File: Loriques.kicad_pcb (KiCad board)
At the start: 4 copper layers, 144.8 x 106.7 mm, 131 parts, among them IC10 MAX17263LETD+T, IC12 TPS22975, IC14 W25Q64FWSSIG, IC19 TPS22975, IC2 MCP73871, IC3 HDC2080, IC4 TPS2013A, IC5 CAT25160VI-GT3, IC6 SN74LVC244A, IC7 LP38691-ADJ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

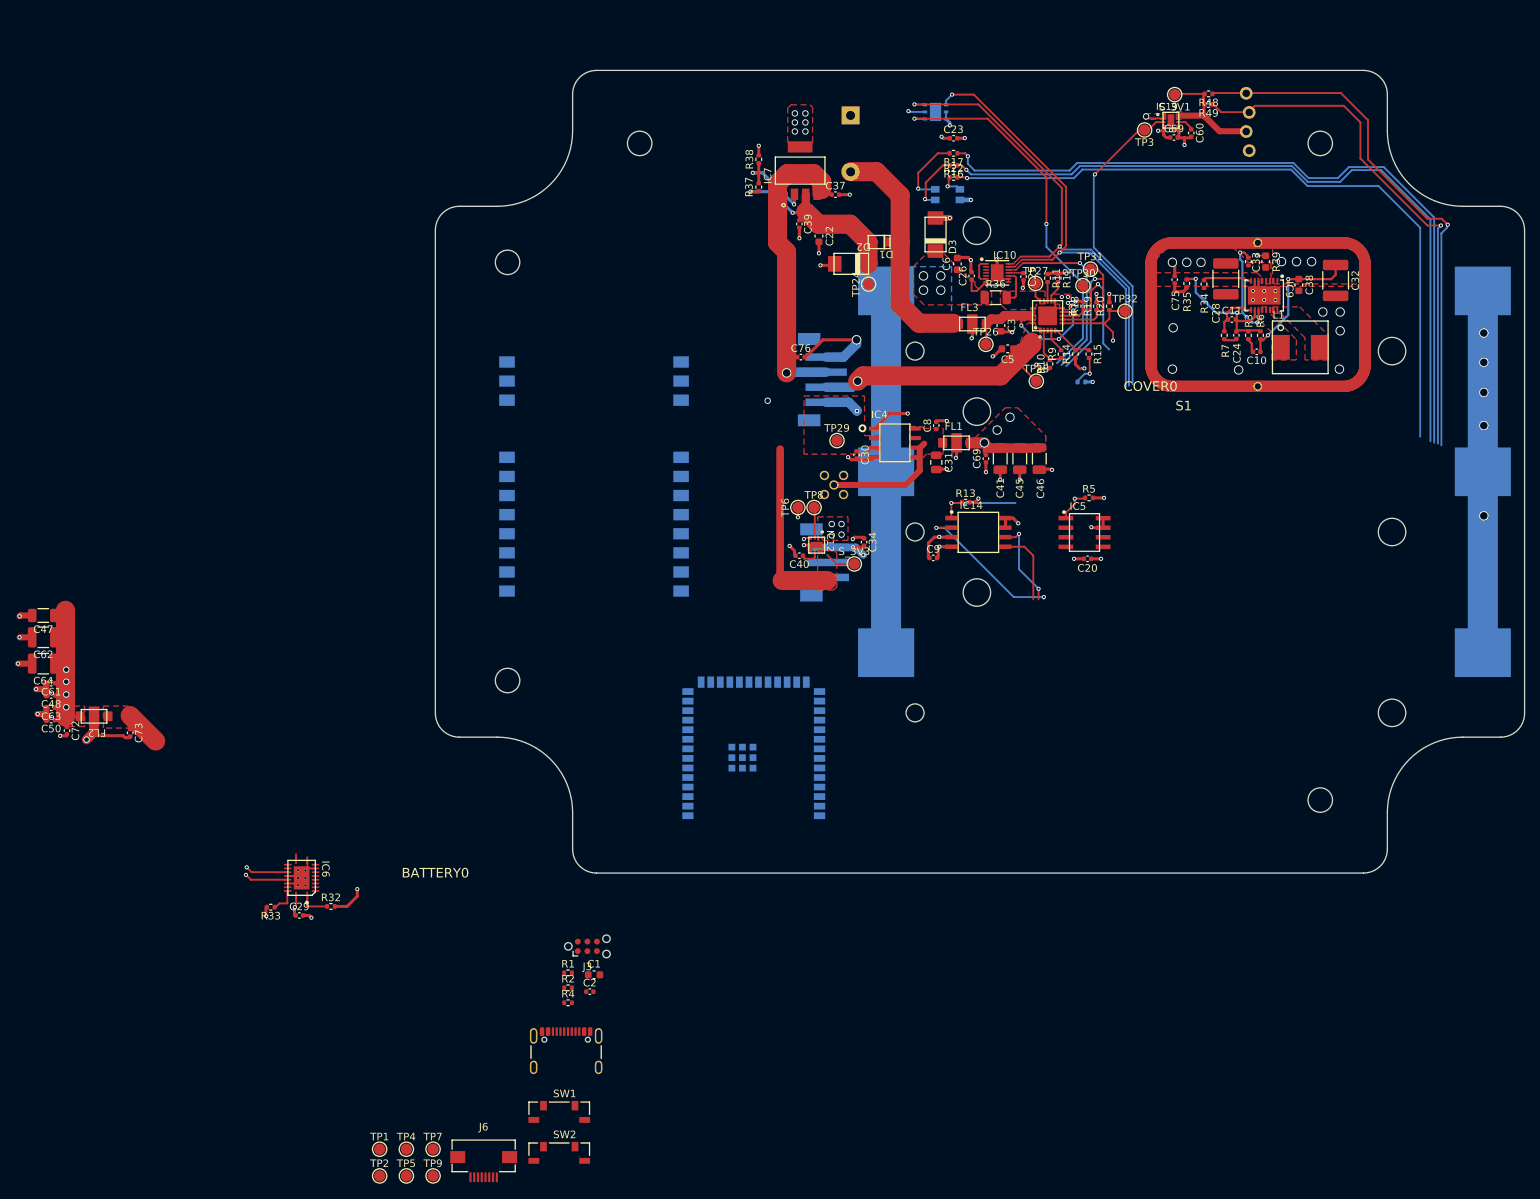
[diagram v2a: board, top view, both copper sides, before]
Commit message: more 3D parts. changed out the temp/humidity sensor for an instock one
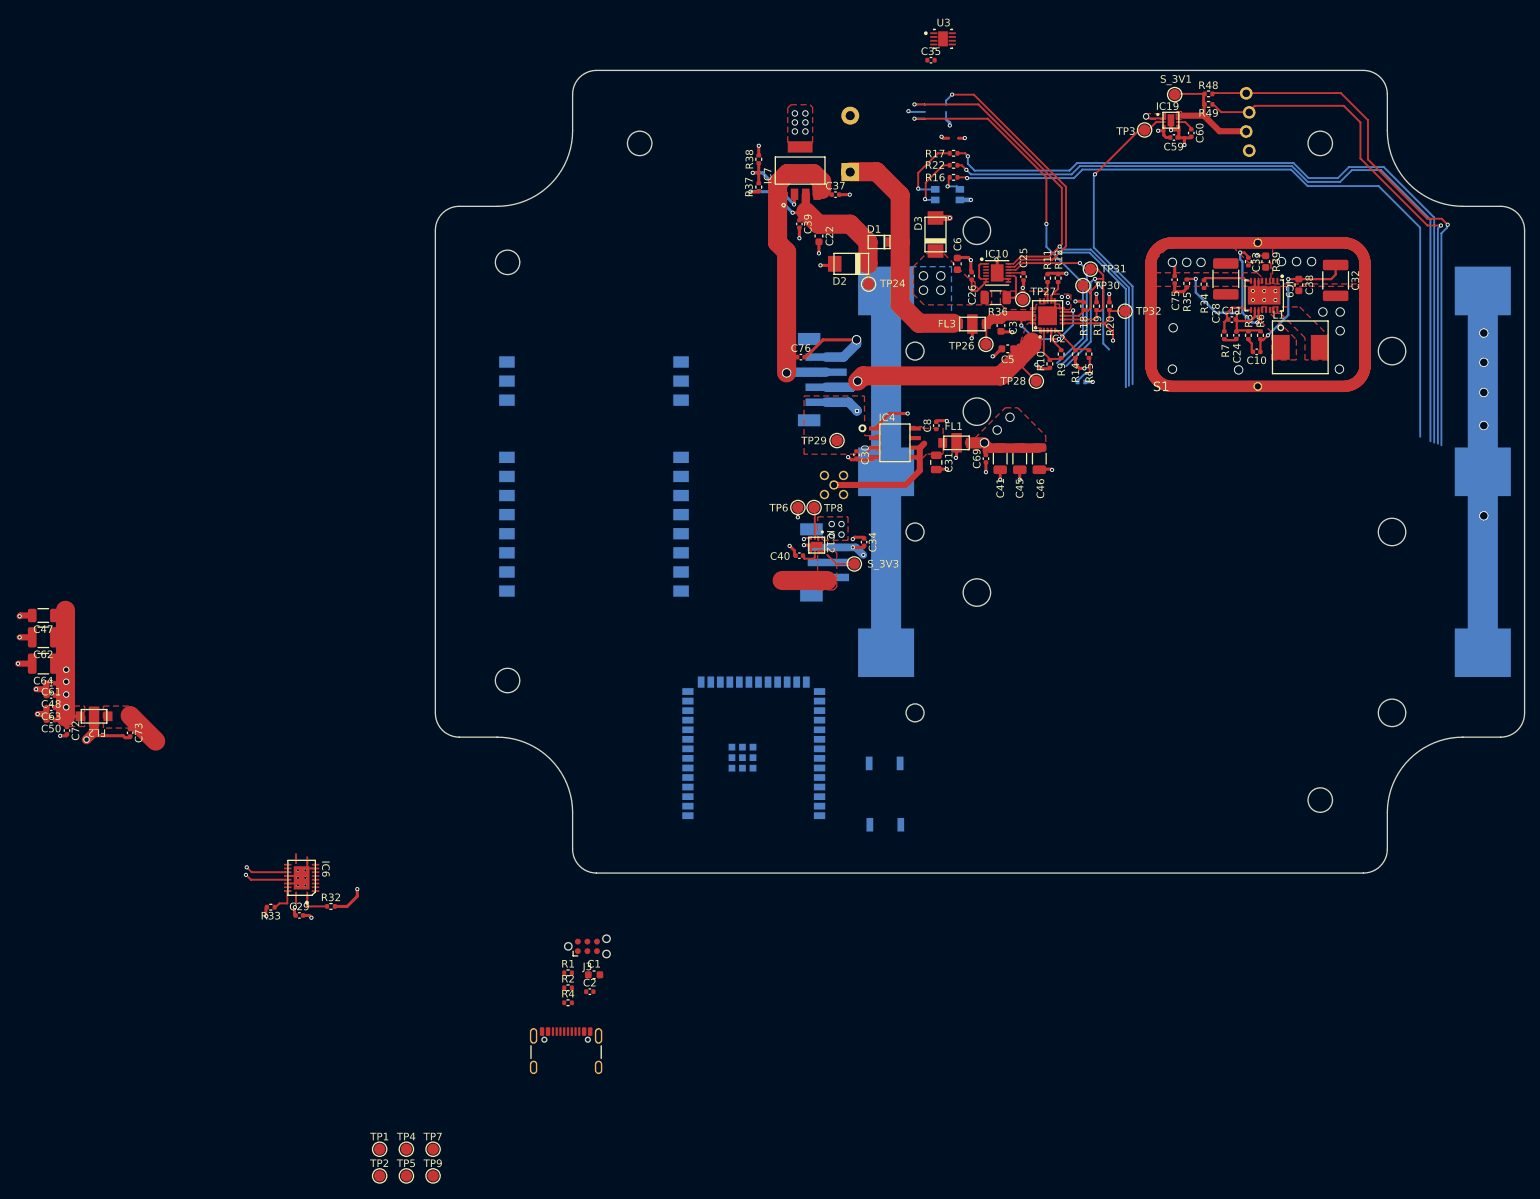
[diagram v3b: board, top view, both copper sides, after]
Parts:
- removed C20, C23, C9: 0.1uF, Capacitor_SMD:C_0402_1005Metric
- removed IC14: W25Q64FWSSIG, Loriques:SOIC127P790X216-8N
- removed IC3: HDC2080, Loriques:DMB0006A
- removed IC5: CAT25160VI-GT3, Loriques:SOIC127P600X175-8N
- removed J6: Conn_01x08, Loriques:FPC-SMD_P0.50-8P_FGS-XJ-H2.0
- removed R13, R5: 100k, Resistor_SMD:R_0402_1005Metric
- added C35: 0.1uF, Capacitor_SMD:C_0402_1005Metric, F.Cu at (142.0, 50.3)
- added U3: HDC3020DEFR, Loriques:DEF0008A-IPC_A, F.Cu at (143.6, 47.4)
- C27: value CPOL_16X27MM -> 4700uF
- SW1, SW2: footprint Loriques:SW_TL3330AF130QG_EWI -> Loriques:SW_CS1213AGF260_CRS; moved to B.Cu
- moved COVER0 73.0 mm to (174.8, 166.6)
- moved SW2 67.9 mm to (135.8, 143.8)
- moved SW1 58.2 mm to (135.9, 151.9)
- moved C27 7.53 mm to (131.2, 65.2), turned to 90 degrees
- moved TP27 2.72 mm to (154.2, 82.1)
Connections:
- C27 pad 1: (no net) -> Net-(C27-Pad1)
- C27 pad 2: (no net) -> GND
- D1 pad K: Net-(C27-Pad+) -> Net-(C27-Pad1)
- FL3 pad 1: Net-(C27-Pad+) -> Net-(C27-Pad1)
- IC6 pad P$11: /Radio/RXEN -> /Radio/RXEN_MCU
- IC6 pad P$12: /Radio/NSS -> /Radio/NSS_RADIO
- IC6 pad P$13: /Radio/TXEN -> /Radio/TXEN_MCU
- IC6 pad P$14: /Radio/SCK -> /Radio/SCK_RADIO
- IC6 pad P$15: /Radio/RST -> /Radio/RST_MCU
- IC6 pad P$16: /Radio/MOSI -> /Radio/MOSI_RADIO
- IC6 pad P$17: /Radio/BUSY -> /Radio/BUSY_RADIO
- IC6 pad P$18: /Radio/MISO -> /Radio/MISO_MCU
- IC6 pad P$2: /Radio/MISO -> /Radio/MISO_RADIO
- IC6 pad P$3: /Radio/BUSY -> /Radio/BUSY_MCU
- IC6 pad P$4: /Radio/MOSI -> /Radio/MOSI_MCU
- IC6 pad P$5: /Radio/RST -> /Radio/RST_RADIO
- IC6 pad P$6: /Radio/SCK -> /Radio/SCK_MCU
- IC6 pad P$7: /Radio/TXEN -> /Radio/TXEN_RADIO
- IC6 pad P$8: /Radio/NSS -> /Radio/NSS_MCU
- IC6 pad P$9: /Radio/RXEN -> /Radio/RXEN_RADIO
- U1 pad 10: /MCU/TX_3V3 -> /MCU/TX_DEBUG_O
- U1 pad 11: /MCU/RX_3V3 -> /MCU/RX_DEBUG_O
- U1 pad 12: unconnected-(U1-GPIO8/TOUCH8/ADC1_CH7/SUBSPICS1-Pad12) -> /MCU/STAT2
- U1 pad 15: unconnected-(U1-GPIO3/TOUCH3/ADC1_CH2*-Pad15) -> /Radio/RXEN_MCU
- U1 pad 17: unconnected-(U1-GPIO9/TOUCH9/ADC1_CH8/FSPIHD/SUBSPIHD-Pad17) -> /MCU/STAT1
- U1 pad 18: unconnected-(U1-GPIO10/TOUCH10/ADC1_CH9/FSPICS0/FSPIIO4/SUBSPICS0-Pad18) -> /Radio/NSS_MCU
- U1 pad 19: unconnected-(U1-GPIO11/TOUCH11/ADC2_CH0/FSPID/FSPIIO5/SUBSPID-Pad19) -> /Radio/MOSI_MCU
- U1 pad 20: unconnected-(U1-GPIO12/TOUCH12/ADC2_CH1/FSPICLK/FSPIIO6/SUBSPICLK-Pad20) -> /Radio/SCK_MCU
- U1 pad 21: unconnected-(U1-GPIO13/TOUCH13/ADC2_CH2/FSPIQ/FSPIIO7/SUBSPIQ-Pad21) -> /Radio/MISO_MCU
- U1 pad 32: Net-(J6-Pin_5) -> unconnected-(U1-MTCK/GPIO39/CLK_OUT3/SUBSPICS1-Pad32)
- U1 pad 33: Net-(J6-Pin_6) -> unconnected-(U1-MTDO/GPIO40/CLK_OUT2-Pad33)
- U1 pad 34: Net-(J6-Pin_7) -> unconnected-(U1-MTDI/GPIO41/CLK_OUT1-Pad34)
- U1 pad 35: Net-(J6-Pin_8) -> unconnected-(U1-MTMS/GPIO42-Pad35)
- U1 pad 38: unconnected-(U1-GPIO2/TOUCH2/ADC1_CH1-Pad38) -> /Radio/BUSY_MCU
- U1 pad 39: /MCU/RST_3V3 -> /Radio/RST_MCU
- U1 pad 4: unconnected-(U1-GPIO4/TOUCH4/ADC1_CH3-Pad4) -> /Radio/TXEN_MCU
- U1 pad 5: unconnected-(U1-GPIO5/TOUCH5/ADC1_CH4-Pad5) -> /FUEL
- U1 pad 6: unconnected-(U1-GPIO6/TOUCH6/ADC1_CH5-Pad6) -> /MCU/RADIO_EN
- U1 pad 7: unconnected-(U1-GPIO7/TOUCH7/ADC1_CH6-Pad7) -> /MCU/PG
- U2 pad 14: /Radio/BUSY -> /Radio/BUSY_RADIO
- U2 pad 15: /Radio/RST -> /Radio/RST_RADIO
- U2 pad 16: /Radio/MISO -> /Radio/MISO_RADIO
- U2 pad 17: /Radio/MOSI -> /Radio/MOSI_RADIO
- U2 pad 18: /Radio/SCK -> /Radio/SCK_RADIO
- U2 pad 19: /Radio/NSS -> /Radio/NSS_RADIO
- U2 pad 6: /Radio/RXEN -> /Radio/RXEN_RADIO
- U2 pad 7: /Radio/TXEN -> /Radio/TXEN_RADIO
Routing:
- net /MCU/DRDY: track 50.4 -> 0.00 mm, vias 2 -> 0
- net (no net): track 0.00 -> 50.4 mm, vias 3 -> 5
- net Net-(C27-Pad1): track 0.00 -> 32.6 mm
- net Net-(C27-Pad+): track 32.6 -> 0.00 mm
- net /MCU/FLASH_MISO: track 20.4 -> 0.00 mm, vias 2 -> 0
- net /Radio/RADIO_3V3: track 33.0 -> 15.8 mm
- net /MCU/3V3: track 73.2 -> 57.8 mm, vias 26 -> 20
- net /MCU/FLASH_CS: track 11.8 -> 0.00 mm, vias 1 -> 0
- net /MCU/FLASH_CLK: track 11.8 -> 0.00 mm, vias 2 -> 0
- net /MCU/FLASH_MOSI: track 9.99 -> 0.00 mm
- net /Radio/MOSI_RADIO: track 0.00 -> 5.85 mm, vias 0 -> 1
- net /Radio/MOSI: track 5.85 -> 0.00 mm, vias 1 -> 0
- net /Radio/SCK_RADIO: track 0.00 -> 5.76 mm, vias 0 -> 1
- net /Radio/SCK: track 5.76 -> 0.00 mm, vias 1 -> 0
- net /MCU/EEPROM_CS: track 4.40 -> 0.00 mm, vias 1 -> 0
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
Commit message: lots of routing, tweaking placement. adding courtyards
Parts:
- removed J5: MMCX-P-P-H-ST-TH1, Loriques:MMCX-P-P-H-ST-TH1
- D2, D3: footprint Loriques:DO-214AC(SMA) -> Diode_SMD:D_SMA
- J3, U3: moved to B.Cu
- L1: value HCMA0703-2R2-R -> 2.2uH; footprint Loriques:HCMA0703-2R2-R -> Loriques:IND_IHLP-2525CZ_VIS
- moved C47 96.1 mm to (119.5, 113.8), turned to 90 degrees
- moved C50 94.4 mm to (117.6, 119.5), turned to -90 degrees
- moved C72 93.7 mm to (118.7, 119.5)
- moved C62 93.5 mm to (116.6, 113.8), turned to 90 degrees
- moved FL2 93.4 mm to (122.0, 118.1)
- moved C73 93.1 mm to (126.8, 121.5)
- moved C63 93.0 mm to (116.5, 119.5), turned to -90 degrees
- moved C48 91.7 mm to (115.4, 119.5), turned to -90 degrees
- moved C64 90.7 mm to (113.1, 113.8), turned to 90 degrees
- moved C61 90.3 mm to (114.3, 119.5), turned to -90 degrees
- moved R33 52.3 mm to (95.8, 131.2)
- moved IC6 51.0 mm to (99.7, 129.2)
- moved C29 50.7 mm to (98.5, 133.4), turned to 180 degrees
- moved R32 47.9 mm to (100.4, 133.9), turned to -90 degrees
- moved J3 41.4 mm to (133.7, 150.4), turned to 90 degrees
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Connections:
- C22 pad 1: Net-(IC7-OUT) -> Net-(D2-A)
- C39 pad 1: Net-(IC7-OUT) -> Net-(D2-A)
- D1 pad A: Net-(IC7-OUT) -> Net-(D2-A)
- IC7 pad 3: Net-(IC7-OUT) -> Net-(D2-A)
- R37 pad 2: Net-(IC7-OUT) -> Net-(D2-A)
- TP24 pad 1: Net-(IC7-OUT) -> Net-(D2-A)
- U1 pad 22: unconnected-(U1-GPIO14/TOUCH14/ADC2_CH3/FSPIWP/FSPIDQS/SUBSPIWP-Pad22) -> /MCU/LED0R
- U1 pad 8: unconnected-(U1-GPIO15/U0RTS/ADC2_CH4/XTAL_32K_P-Pad8) -> /MCU/LED0G
- U1 pad 9: unconnected-(U1-GPIO16/U0CTS/ADC2_CH5/XTAL_32K_NH5-Pad9) -> /MCU/LED0B
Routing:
- net GND: track 177.3 -> 89.1 mm, vias 64 -> 184
- net /MCU/LED0R: track 92.9 -> 25.8 mm
- net /MCU/LED0G: track 99.4 -> 35.4 mm
- net /MCU/LED0B: track 97.4 -> 33.5 mm
- net /Radio/RST_MCU: track 0.00 -> 51.8 mm, vias 0 -> 3
- net /Voltage Regulator/VOUT_FILTERED: track 52.4 -> 1.33 mm, vias 6 -> 65
- net (no net): track 50.4 -> 0.00 mm, vias 5 -> 0
- net /MCU/RADIO_EN: track 4.09 -> 53.4 mm, vias 0 -> 3
- net /Power Input/PANEL_IN: track 45.3 -> 0.00 mm, vias 1 -> 30
- net /SCL: track 135.4 -> 90.9 mm, vias 3 -> 2
- net /Radio/MISO_MCU: track 0.01 -> 43.6 mm, vias 0 -> 3
- net /Radio/MISO_RADIO: track 0.00 -> 42.5 mm, vias 0 -> 1
- net /SDA: track 133.7 -> 92.4 mm, vias 3 -> 2
- net /Radio/BUSY_MCU: track 0.00 -> 40.2 mm, vias 0 -> 3
- net /Radio/RST_RADIO: track 0.00 -> 37.2 mm, vias 0 -> 1
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- added copper zone on F.Cu, net /MCU/DISP_3V3
- added copper zone on F.Cu, net /Power Input/CHARGE_IN
- added copper zone on B.Cu, net /Power Input/PANEL_IN
- added copper zone on F.Cu, net /Power Input/PANEL_IN
- added copper zone on B.Cu, net /Power Input/VOUT
- added copper zone on B.Cu, net /Power Input/VOUT_S1
- added copper zone on B.Cu, net /Voltage Regulator/VOUT_FILTERED
- added copper zone on B.Cu, net GND
- added copper zone on F.Cu, net Net-(C27-Pad1)
- added copper zone on F.Cu, net Net-(D2-A)
- added copper zone on B.Cu, net VCC
- removed copper zone on F.Cu, net (none)
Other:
- copper layers 4 -> 6
